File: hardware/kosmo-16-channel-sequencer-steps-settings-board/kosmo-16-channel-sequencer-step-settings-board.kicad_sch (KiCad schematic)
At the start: 98 parts, among them J14 STEP-SETTINGS-ANGLED, SW29 NOTE1, SW30 NOTE2, SW31 NOTE3, SW32 NOTE4, SW33 LENGTH, SW34 VOLUME, SW35 CC1, SW36 CC2, SW37 CC3, SW38 ENV, SW39 PC, SW40 TRIGGER, U10 74HC165, U28 MAX7219, U29 MAX7219, U30 MAX7219, U31 MAX7219, U32 MAX7219, U5 MAX7219, U6 74HC165, U7 74HC165, U8 74HC165, U9 74HC165

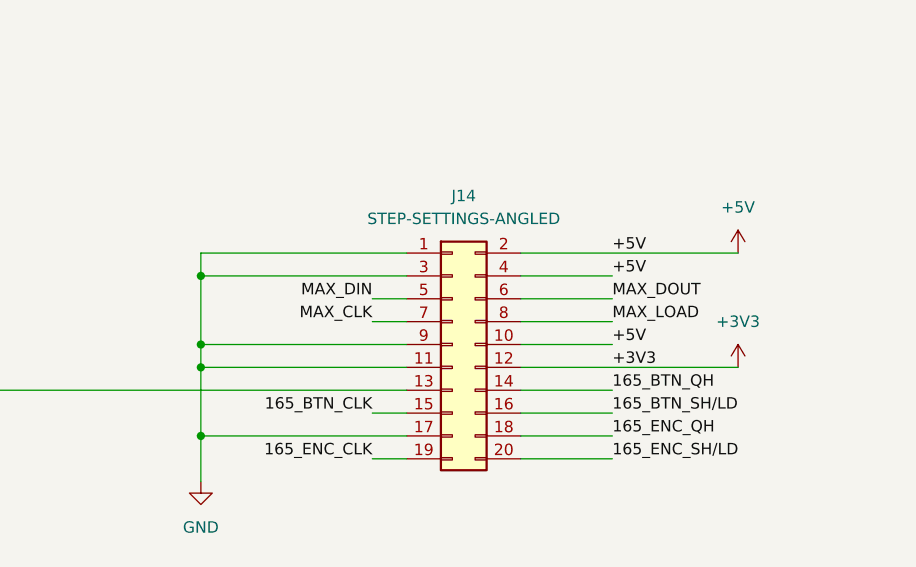
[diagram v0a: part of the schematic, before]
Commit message: added pcb labels
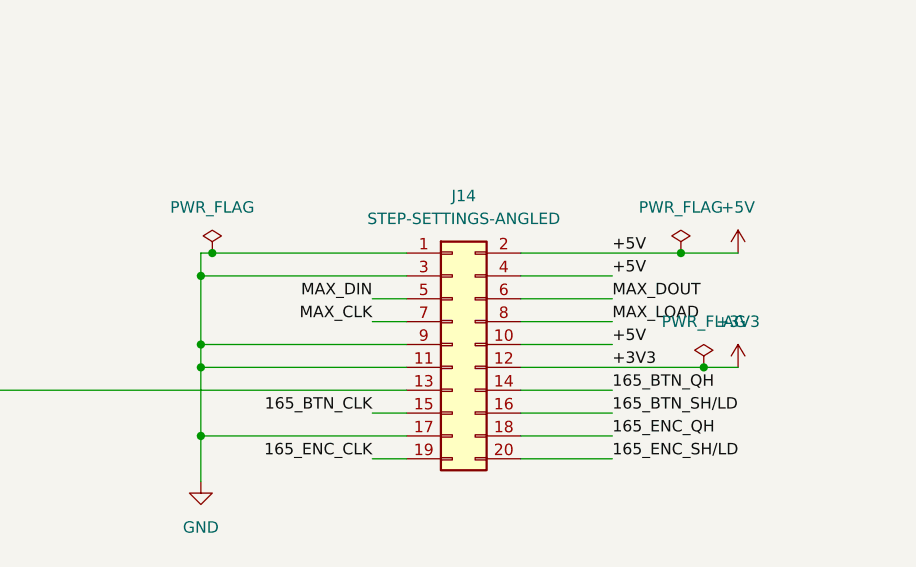
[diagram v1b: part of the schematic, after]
